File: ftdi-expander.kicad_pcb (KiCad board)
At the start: 2 copper layers, 23 x 38 mm, 17 parts, among them J1 Conn_01x10, J2 Conn_01x10, J3 ARM-JTAG-10, J4 IDC 02x04, J5 AVR-ISP-6, J6 Conn_01x06_Male, SW1 SW_SPDT, SW2 SW_SPDT, U1 AZ1117EH-3.3TRG1

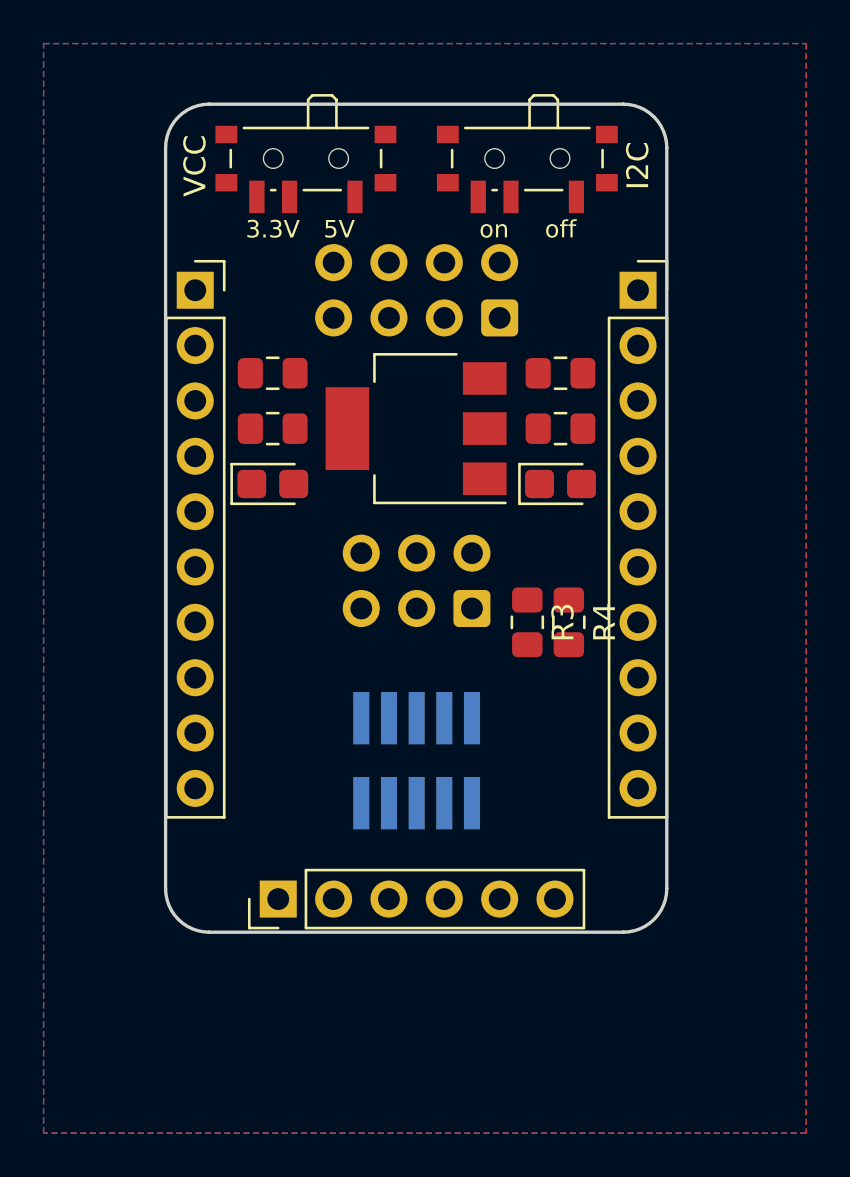
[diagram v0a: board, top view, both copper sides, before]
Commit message: routed version with spdt switches
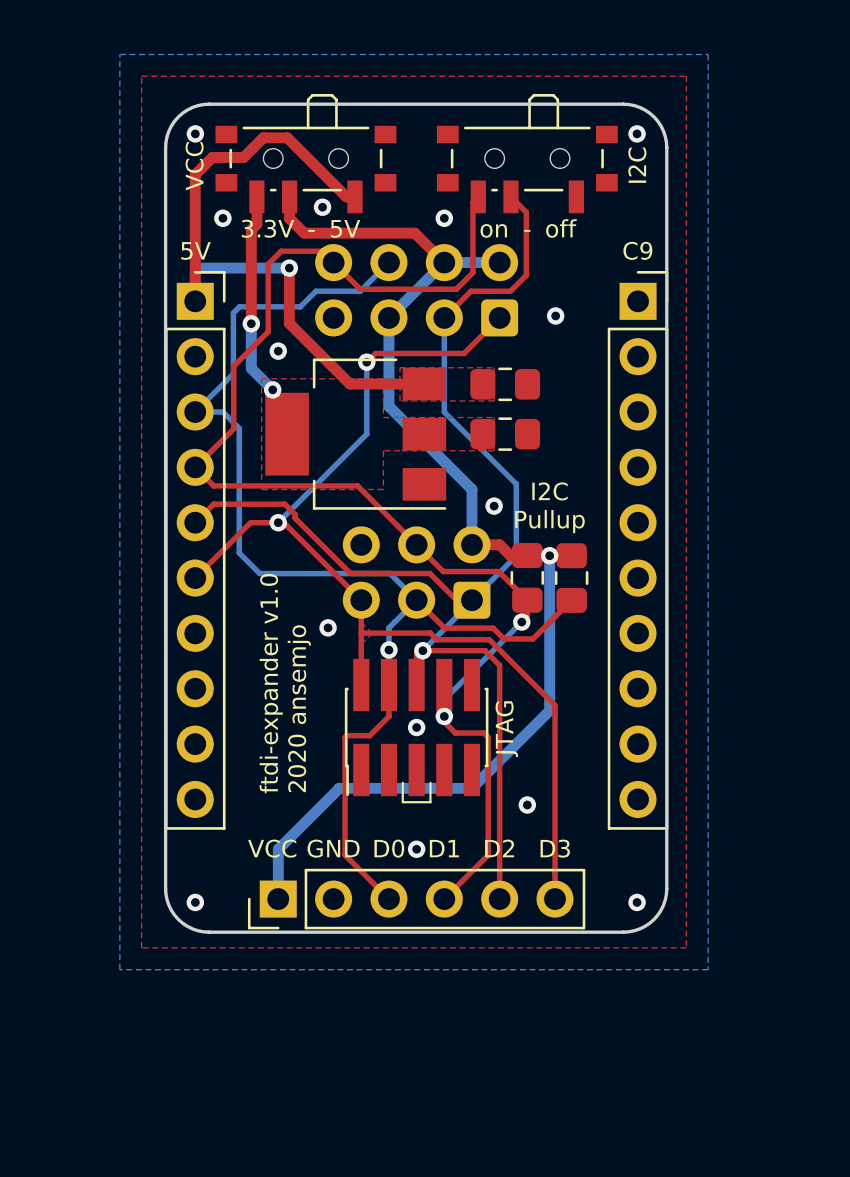
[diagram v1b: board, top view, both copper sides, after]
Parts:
- removed D1: GREEN, LED_SMD:LED_0805_2012Metric_Castellated
- removed D2: RED, LED_SMD:LED_0805_2012Metric_Castellated
- removed R1: 1kΩ, Resistor_SMD:R_0805_2012Metric_Pad1.15x1.40mm_HandSolder
- removed R2: 2.2kΩ, Resistor_SMD:R_0805_2012Metric_Pad1.15x1.40mm_HandSolder
- J3: moved to F.Cu
- moved C2 11.0 mm to (138.7, 90.4), turned to 180 degrees
- moved U1 2.78 mm to (131.8, 90.4)
- moved C1 2.59 mm to (138.7, 88.1)
- moved R3 2.04 mm to (139.7, 97.0)
- moved R4 2.04 mm to (141.7, 97.0)
- moved J3 1.52 mm to (134.6, 103.9)
- moved J1 0.51 mm to (124.5, 84.3)
- moved J2 0.51 mm to (144.8, 84.3)
- moved J5 0.38 mm to (137.2, 98.0)
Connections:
- SW2 pad 2: D1 -> D2
- SW2 pad 3: D2 -> D1
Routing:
- net D1: track 0.00 -> 61.9 mm, vias 0 -> 2
- net D2: track 0.00 -> 58.2 mm, vias 0 -> 1
- net VCC: track 0.00 -> 56.3 mm, vias 0 -> 1
- net D0: track 0.00 -> 55.6 mm, vias 0 -> 1
- net D3: track 0.00 -> 49.2 mm, vias 0 -> 2
- net +5V: track 0.00 -> 30.8 mm, vias 0 -> 1
- net +3V3: track 0.00 -> 9.37 mm, vias 0 -> 2
- net GND: vias 0 -> 14
- added copper zone on F.Cu, net +3V3
- added copper zone on F.Cu, net +5V
- added copper zone on F.Cu, net D3
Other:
- board text added: "-"
- board text added: "AVR ICSP"
- board text added: "Adafruit FT232H Expander"
- board text added: "C9"
- board text added: "CIPO"
- board text added: "CLK"
- board text added: "COPI"
- board text added: "CS"
- board text added: "CTS"
- board text added: "D0"
- board text added: "D1"
- board text added: "D2"
- board text added: "D3"
- board text added: "Flash Programmer"
- board text added: "GND"
- board text added: "I2C Pullup"
- board text added: "JTAG"
- board text added: "RTS"
- board text added: "RX"
- board text added: "SCK"
- board text added: "SCL"
- board text added: "SDA"
- board text added: "SPI"
- board text added: "Serial"
- board text added: "TCK"
- board text added: "TDI"
- board text added: "TDO"
- board text added: "TMS"
- board text added: "TX"
- board text added: "ftdi-expander v1.0 2020 ansemjo"
- board text added: "~CS~"
- board text added: "~HOLD~"
- board text added: "~RST~"
- board text added: "~WP~"

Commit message: replaced switches with jumper headers, tidied up traces, added teardrops
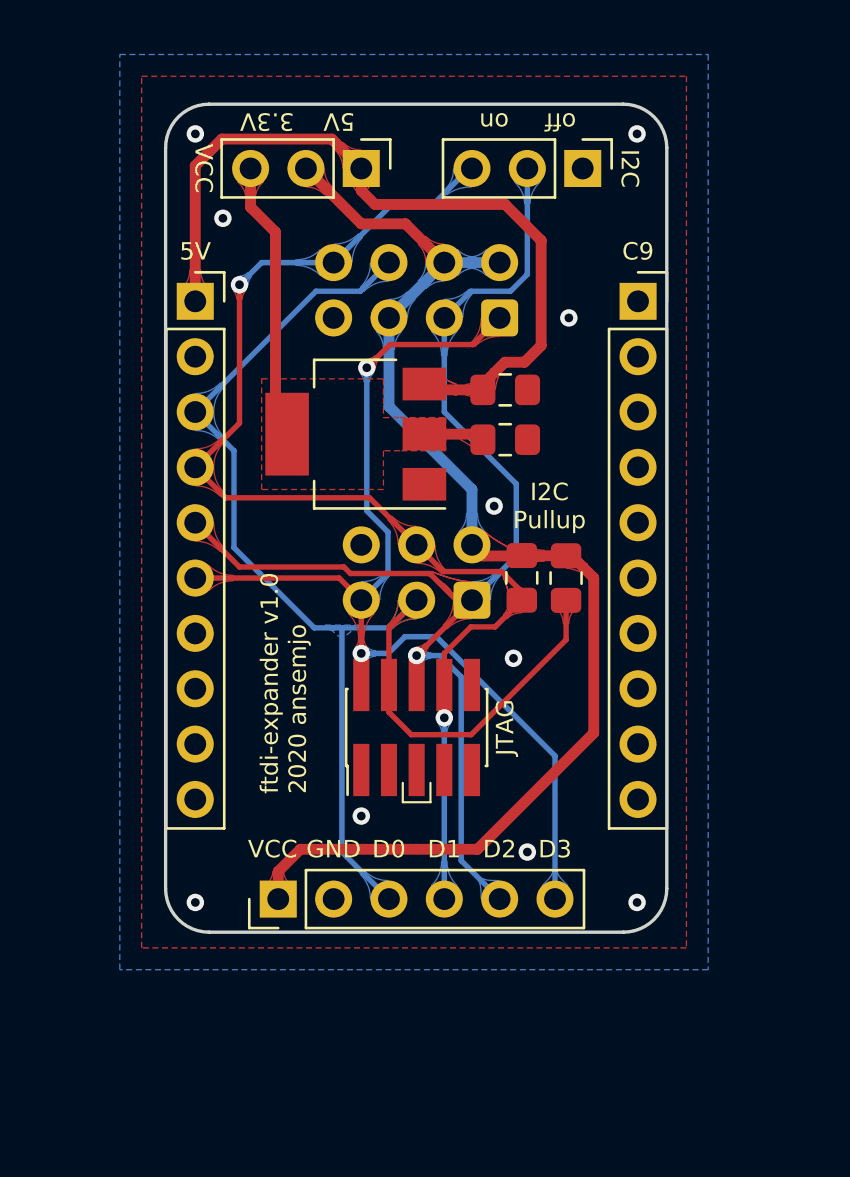
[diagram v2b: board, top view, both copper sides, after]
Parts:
- SW1, SW2: value SW_SPDT -> Jumper; footprint Button_Switch_SMD:SW_SPDT_PCM12 -> Connector_PinHeader_2.54mm:PinHeader_1x03_P2.54mm_Vertical
- moved SW1 2.54 mm to (132.1, 78.2), turned to 270 degrees
- moved SW2 2.54 mm to (142.2, 78.2), turned to 270 degrees
- moved C1 0.25 mm to (138.7, 88.4)
- moved C2 0.25 mm to (138.7, 90.7)
- moved R3 0.25 mm to (139.4, 97.0)
- moved R4 0.25 mm to (141.5, 97.0)
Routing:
- net +3V3: track 9.37 -> 15.9 mm, vias 2 -> 0
- net D1: track 61.9 -> 55.7 mm
- net +5V: track 30.8 -> 36.4 mm, vias 1 -> 0
- net D0: track 55.6 -> 60.4 mm, vias 1 -> 0
- net VCC: track 56.3 -> 58.0 mm, vias 1 -> 0
- net D2: track 58.2 -> 57.3 mm
- net D3: track 49.2 -> 48.6 mm
- net GND: vias 14 -> 10
- added copper zone on B.Cu, net D0
- removed copper zone on F.Cu, net +5V
- removed copper zone on F.Cu, net D3
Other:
- board text removed: "-"

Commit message: fixed some drc errors caused by teardrops
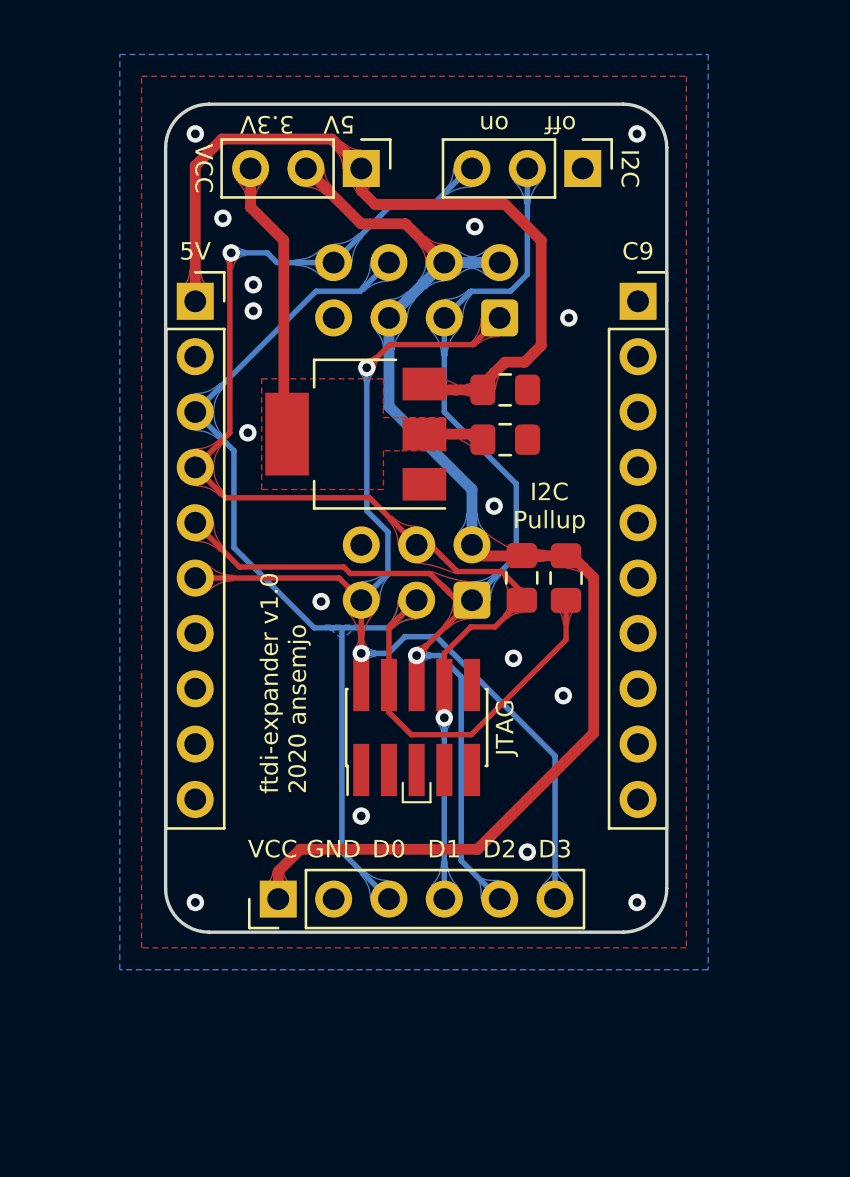
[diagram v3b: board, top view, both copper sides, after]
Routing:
- net D1: track 55.7 -> 57.2 mm
- net GND: vias 10 -> 16
